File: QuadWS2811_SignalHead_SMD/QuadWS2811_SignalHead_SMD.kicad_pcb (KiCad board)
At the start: 2 copper layers, 94.8 x 20.4 mm, 29 parts, among them K1 GND In +5, K2 GND Out +5, P1 C Y G R, P2 C Y G R, P3 C Y G R, P4 C Y G R, U1 WS2811, U2 WS2811, U3 WS2811, U4 WS2811

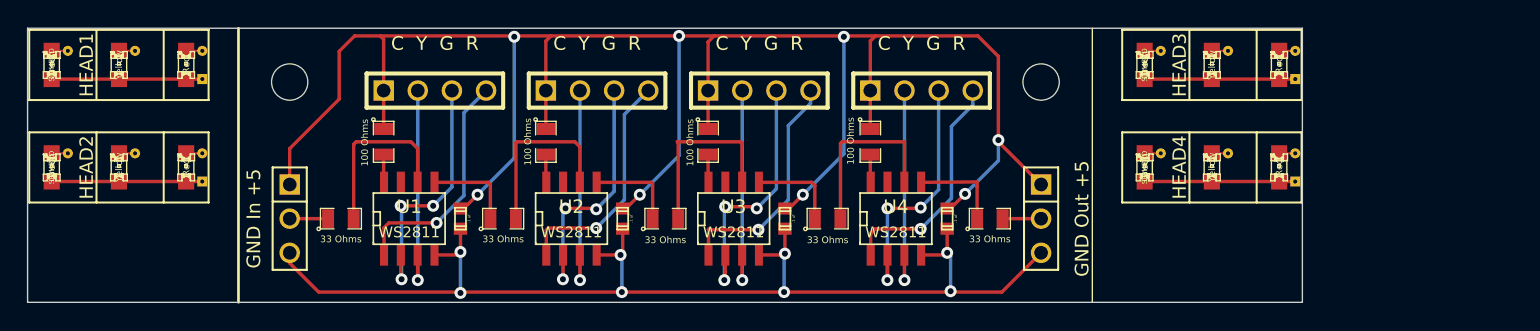
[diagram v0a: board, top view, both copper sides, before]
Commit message: Add dummy head driver (just series resistors) and dummy heads.
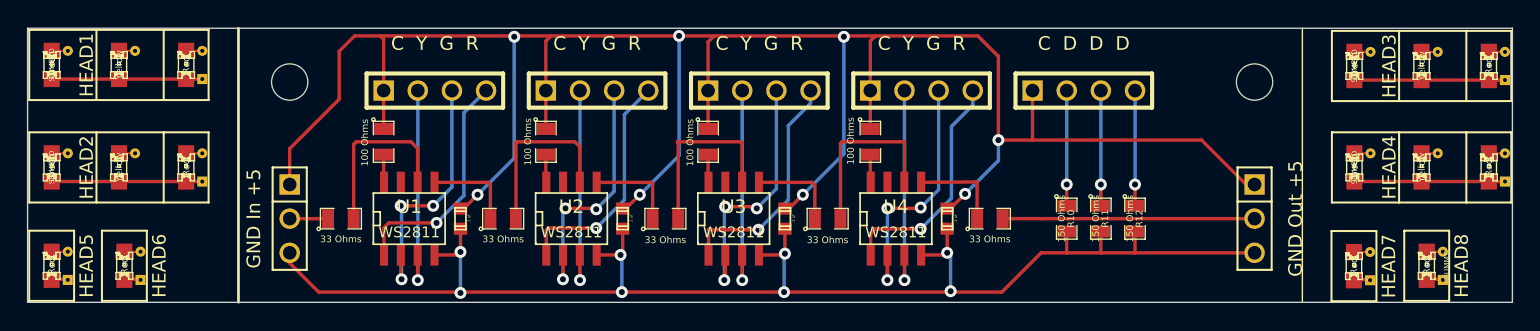
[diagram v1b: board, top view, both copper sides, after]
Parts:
- added HEAD5: DUMMY, SH1, F.Cu at (115.6, 119.1)
- added HEAD6: DUMMY, SH1, F.Cu at (121.1, 119.1)
- added HEAD7: DUMMY, SH1, F.Cu at (212.5, 119.1)
- added HEAD8: DUMMY, SH1, F.Cu at (217.9, 119.1)
- added P5: C D D D, ScrewTerm_2.54-4, F.Cu at (192.4, 106.0)
- added R10: 150 Ohms, SM0805, F.Cu at (191.1, 115.6)
- added R11: 150 Ohms, SM0805, F.Cu at (193.7, 115.6)
- added R12: 150 Ohms, SM0805, F.Cu at (196.2, 115.6)
- moved K2 15.9 mm to (205.1, 115.6)
- moved MH 15.9 mm to (205.1, 105.4)
- moved HEAD3 15.6 mm to (217.5, 104.2)
- moved HEAD4 15.6 mm to (217.5, 111.8)
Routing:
- net GND: track 86.1 -> 106.8 mm
- net +5V: track 151.9 -> 171.6 mm
- net N-0000043: track 2.86 -> 18.7 mm
- net N-0000012: track 0.00 -> 8.57 mm, vias 0 -> 1
- net N-0000011: track 0.00 -> 8.57 mm, vias 0 -> 1
- net N-0000010: track 0.00 -> 8.57 mm, vias 0 -> 1
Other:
- board size 94.8 x 20.4 mm -> 110.4 x 20.4 mm
